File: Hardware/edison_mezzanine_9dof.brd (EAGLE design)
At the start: 30.5 x 44.5 mm, 37 parts, among them U1 LSM9DS0, U2 EDISON_CONNECTOR_FULLMOUNTING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, U3 EDISON_CONNECTOR_FULLHEADER

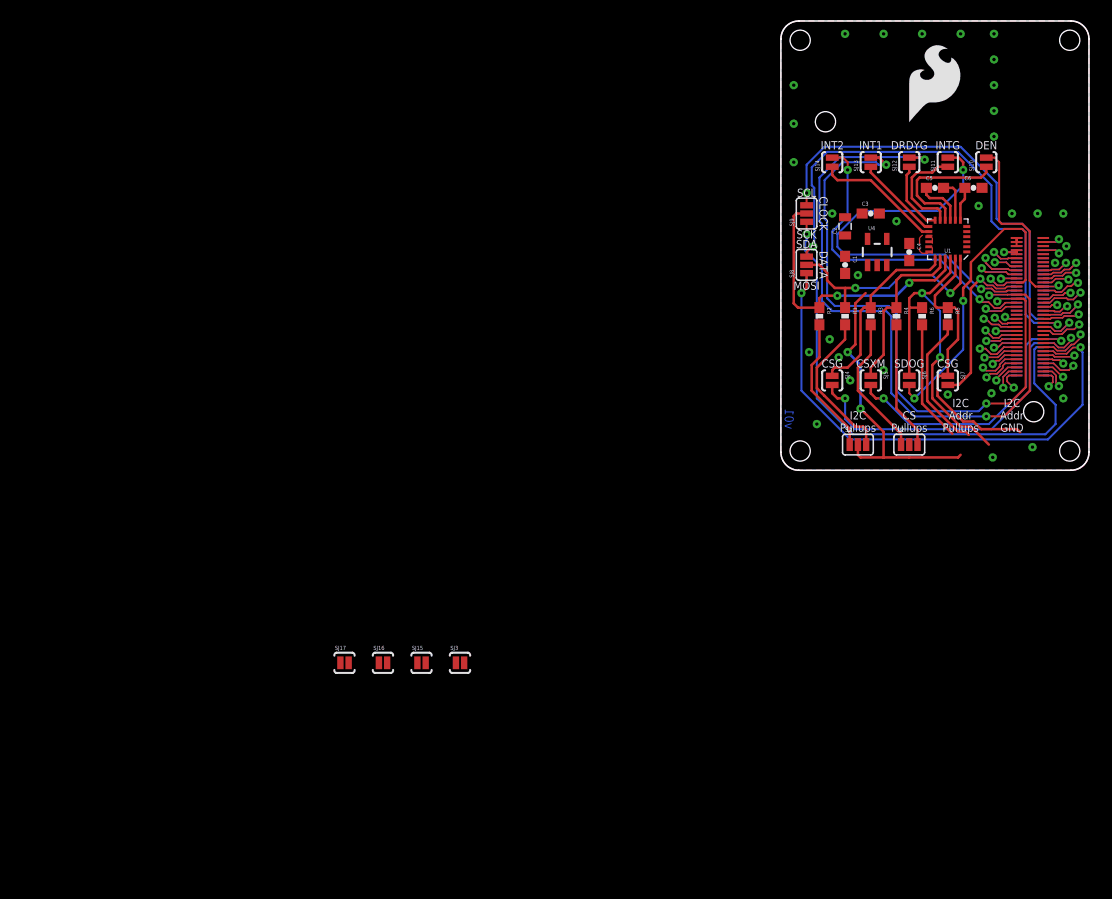
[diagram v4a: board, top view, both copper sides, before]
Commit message: Re-did power section to include LDO. Added 4x 2-way jumpers to layout for pullups/pulldowns.
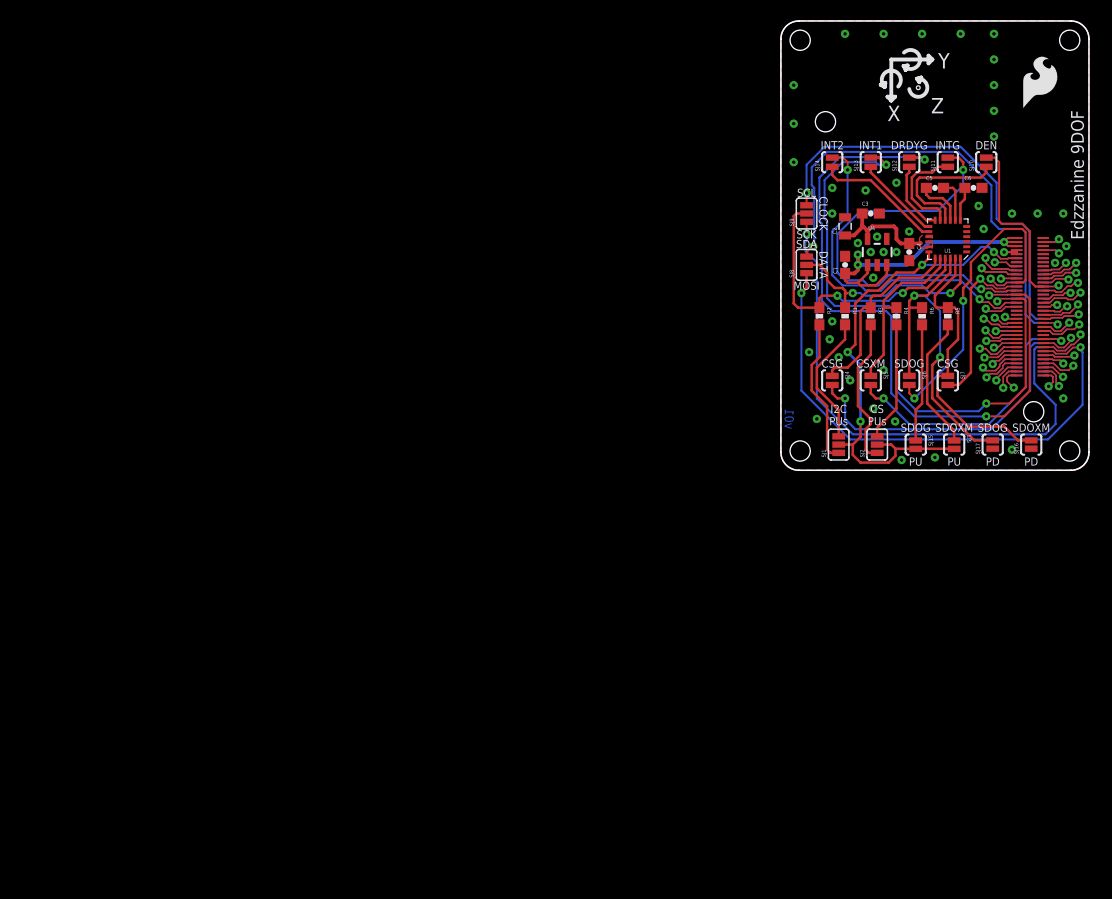
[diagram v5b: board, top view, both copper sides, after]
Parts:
- LOGO1: value SFE_LOGO_FLAME.3_INCH -> SFE_LOGO_FLAME.2_INCH; device SparkFun-Aesthetics:SFE_LOGO_FLAME_.3 -> SparkFun-Aesthetics:SFE_LOGO_FLAME_.2
- moved SJ16 67.7 mm to (24.8, 2.54), turned to 90 degrees
- moved SJ17 67.7 mm to (21.0, 2.54), turned to 90 degrees
- moved SJ15 53.4 mm to (13.3, 2.54), turned to 270 degrees
- moved SJ3 53.4 mm to (17.1, 2.54), turned to 270 degrees
- moved LOGO1 11.5 mm to (23.6, 35.6)
- moved SJ2 3.17 mm to (9.53, 2.54), turned to 90 degrees
- moved SJ1 1.91 mm to (5.71, 2.54), turned to 90 degrees
- turned C1 to 90 degrees
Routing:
- net VSYS: track 1.20 -> 36.1 mm, vias 0 -> 3
- net 1.8V: track 34.9 -> 53.7 mm, vias 3 -> 4
- net 3.3V_LOCAL: track 0.00 -> 11.6 mm
- net N$6: track 15.5 -> 13.1 mm
- net GP49: track 36.1 -> 38.4 mm
- net GP46: track 43.1 -> 45.4 mm
- net SDO_XM: track 27.4 -> 28.9 mm
- net N$5: track 12.7 -> 11.8 mm
- net N$7: track 13.7 -> 14.6 mm
- net N$4: track 14.1 -> 14.9 mm
- net SDO_G: track 34.4 -> 35.2 mm
- net SDA: track 22.7 -> 22.1 mm
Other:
- board text added: "CS PUs"
- board text added: "I2C PUs"
- board text added: "PD"
- board text added: "PU"
- board text added: "SDOXM"
- board text added: "X"
- board text added: "Y"
- board text added: "Z"
- board text removed: "CS Pullups"
- board text removed: "I2C Addr GND"
- board text removed: "I2C Addr Pullups"
- board text removed: "I2C Pullups"

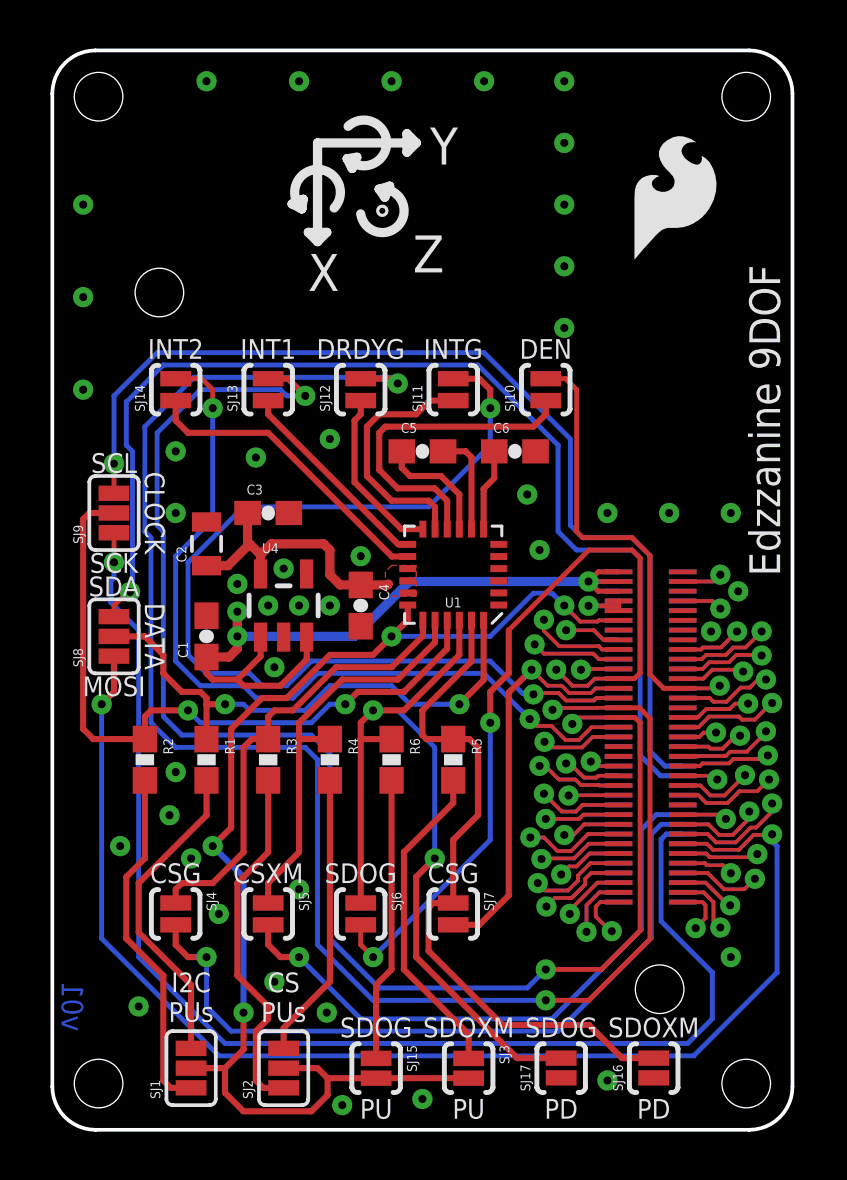
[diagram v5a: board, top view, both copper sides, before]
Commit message: Added fiducials and moved ver text on layout. Moved address table near pullups/pulldowns on schematic.
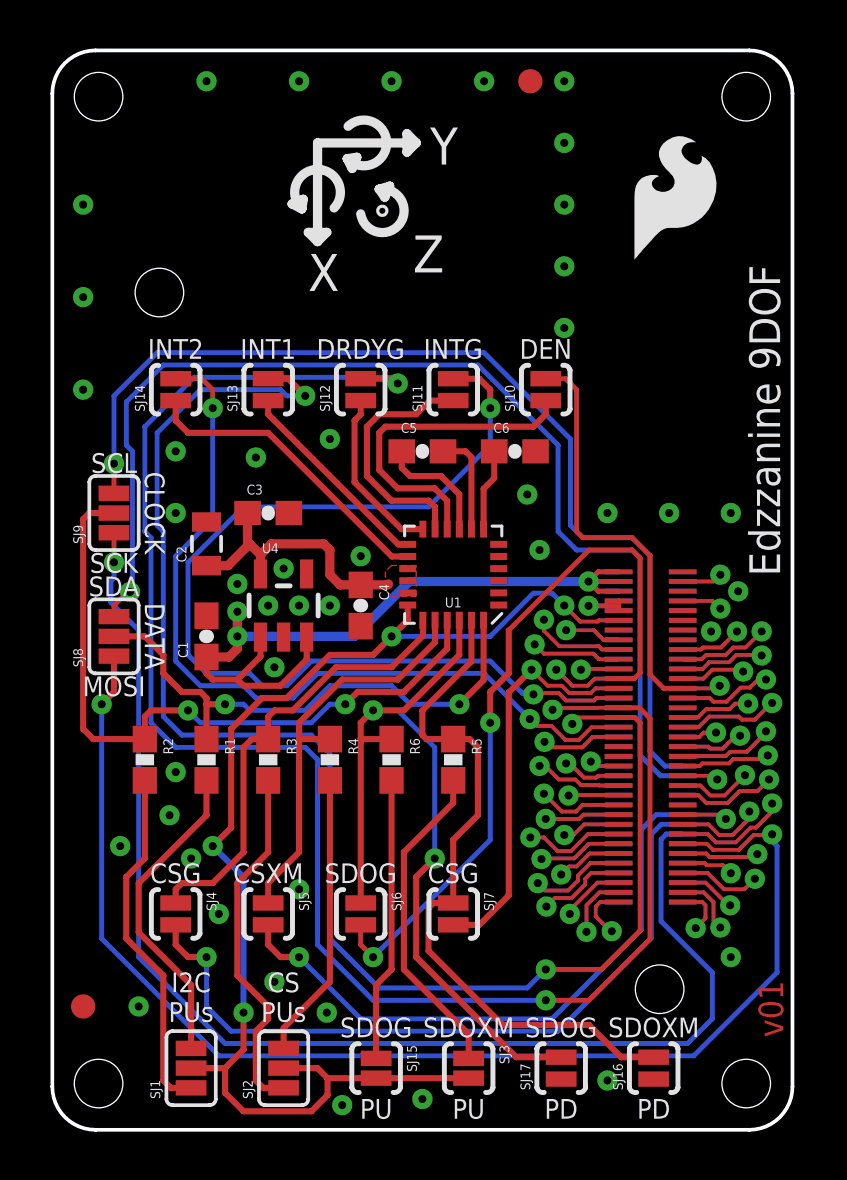
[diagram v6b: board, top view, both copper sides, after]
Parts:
- added FID1, FID2: FIDUCIAL1X2, SparkFun-Aesthetics:FIDUCIAL-1X2
- added FRAME2, FRAME3: FRAME-LETTER, SparkFun-Aesthetics:CREATIVE_COMMONS
- SJ16, SJ17: value JUMPER-PAD-2-NC_BY_PASTE -> JUMPER-PAD-2-NOYES_SILK; device SparkFun-Passives:PAD-JUMPER-2-NC_BY_PASTE_YES_SILK -> SparkFun-Passives:PAD-JUMPER-2-NO_YES_SILK
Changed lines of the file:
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@@
 <layer number="2" name="Route2" color="1" fill="3" visible="no" active="yes"/>
 <layer number="15" name="Route15" color="4" fill="6" visible="no" active="yes"/>
-<layer number="16" name="Bottom" color="1" fill="1" visible="no" active="yes"/>
+<layer number="16" name="Bottom" color="1" fill="1" visible="yes" active="yes"/>
 <layer number="17" name="Pads" color="2" fill="1" visible="yes" active="yes"/>
 <layer number="18" name="Vias" color="2" fill="1" visible="yes" active="yes"/>
@@
 <layer number="20" name="Dimension" color="15" fill="1" visible="yes" active="yes"/>
 <layer number="21" name="tPlace" color="16" fill="1" visible="yes" active="yes"/>
-<layer number="22" name="bPlace" color="14" fill="1" visible="no" active="yes"/>
+<layer number="22" name="bPlace" color="14" fill="1" visible="yes" active="yes"/>
 <layer number="23" name="tOrigins" color="15" fill="1" visible="yes" active="yes"/>
-<layer number="24" name="bOrigins" color="15" fill="1" visible="no" active="yes"/>
+<layer number="24" name="bOrigins" color="15" fill="1" visible="yes" active="yes"/>
 <layer number="25" name="tNames" color="7" fill="1" visible="no" active="yes"/>
 <layer number="26" name="bNames" color="7" fill="1" visible="no" active="yes"/>
@@
 <layer number="43" name="vRestrict" color="2" fill="10" visible="no" active="yes"/>
 <layer number="44" name="Drills" color="7" fill="1" visible="no" active="yes"/>
-<layer number="45" name="Holes" color="7" fill="1" visible="no" active="yes"/>
+<layer number="45" name="Holes" color="7" fill="1" visible="yes" active="yes"/>
 <layer number="46" name="Milling" color="3" fill="1" visible="no" active="yes"/>
-<layer number="51" name="tDocu" color="6" fill="1" visible="no" active="yes"/>
+<layer number="51" name="tDocu" color="6" fill="1" visible="yes" active="yes"/>
 <layer number="52" name="bDocu" color="7" fill="1" visible="no" active="yes"/>
 <layer number="3" name="Route3" color="4" fill="3" visible="no" active="no"/>
@@
 <text x="29.21" y="6.35" size="1.016" layer="22" font="vector" ratio="15" rot="MR90" align="center">4xM2.0</text>
 <rectangle x1="15.24" y1="21.59" x2="17.78" y2="24.13" layer="41"/>
-<text x="1.27" y="5.08" size="0.889" layer="16" font="vector" ratio="15" rot="MR90" align="top-center">v01</text>
-<rectangle x1="0.254" y1="4.318" x2="0.508" y2="4.572" layer="42"/>
 <text x="5.715" y="4.445" size="0.8128" layer="21" font="vector" ratio="15" align="bottom-center">I2C
 PUs</text>
@@
 <wire x1="14.605" y1="40.259" x2="14.605" y2="41.021" width="0.381" layer="21"/>
 <wire x1="14.986" y1="40.64" x2="14.605" y2="40.259" width="0.381" layer="21"/>
+<text x="30.099" y="3.81" size="1.016" layer="1" font="vector" ratio="14" rot="R90">v01</text>
 </plain>
 <attributes>
@@
 <element name="SJ3" library="SparkFun-Passives" package="PAD-JUMPER-2-NC_BY_PASTE_YES_SILK" value="JUMPER-PAD-2-NC_BY_PASTE" x="17.145" y="2.54" rot="R270"/>
 <element name="SJ15" library="SparkFun-Passives" package="PAD-JUMPER-2-NC_BY_PASTE_YES_SILK" value="JUMPER-PAD-2-NC_BY_PASTE" x="13.335" y="2.54" rot="R270"/>
-<element name="SJ16" library="SparkFun-Passives" package="PAD-JUMPER-2-NC_BY_PASTE_YES_SILK" value="JUMPER-PAD-2-NC_BY_PASTE" x="24.765" y="2.54" rot="R90"/>
-<element name="SJ17" library="SparkFun-Passives" package="PAD-JUMPER-2-NC_BY_PASTE_YES_SILK" value="JUMPER-PAD-2-NC_BY_PASTE" x="20.955" y="2.54" rot="R90"/>
 <element name="LOGO1" library="SparkFun-Aesthetics" package="SFE_LOGO_FLAME_.2" value="SFE_LOGO_FLAME.2_INCH" x="23.622" y="35.56"/>
+<element name="FID1" library="SparkFun-Aesthetics" package="FIDUCIAL-1X2" value="FIDUCIAL1X2" x="1.27" y="5.08"/>
+<element name="FID2" library="SparkFun-Aesthetics" package="FIDUCIAL-1X2" value="FIDUCIAL1X2" x="19.685" y="43.18"/>
+<element name="FRAME2" library="SparkFun-Aesthetics" package="CREATIVE_COMMONS" value="FRAME-LETTER" x="-8.89" y="-20.32"/>
+<element name="FRAME3" library="SparkFun-Aesthetics" package="CREATIVE_COMMONS" value="FRAME-LETTER" x="-8.89" y="-20.32"/>
+<element name="SJ16" library="SparkFun-Passives" package="PAD-JUMPER-2-NO_YES_SILK" value="JUMPER-PAD-2-NOYES_SILK" x="24.765" y="2.54" rot="R90"/>
+<element name="SJ17" library="SparkFun-Passives" package="PAD-JUMPER-2-NO_YES_SILK" value="JUMPER-PAD-2-NOYES_SILK" x="20.955" y="2.54" rot="R90"/>
 </elements>
 <signals>
@@
 <via x="22.86" y="25.4" extent="1-16" drill="0.3302"/>
 <via x="19.558" y="26.162" extent="1-16" drill="0.3302"/>
-<contactref element="SJ16" pad="1"/>
-<contactref element="SJ17" pad="1"/>
 <via x="8.89" y="21.59" extent="1-16" drill="0.3302"/>
 <via x="10.16" y="21.59" extent="1-16" drill="0.3302"/>
@@
 <via x="5.08" y="14.732" extent="1-16" drill="0.3302"/>
 <via x="20.066" y="23.876" extent="1-16" drill="0.3302"/>
+<contactref element="SJ16" pad="1"/>
+<contactref element="SJ17" pad="1"/>
 </signal>
 <signal name="VSYS">
@@
 <wire x1="13.97" y1="16.09" x2="12.7136" y2="16.09" width="0.254" layer="1"/>
 <wire x1="12.7136" y1="16.09" x2="12.7" y2="16.1036" width="0.254" layer="1"/>
-<contactref element="SJ17" pad="2"/>
-<wire x1="20.955" y1="2.9527" x2="19.1453" y2="2.9527" width="0.254" layer="1"/>
-<wire x1="19.1453" y1="2.9527" x2="14.986" y2="7.112" width="0.254" layer="1"/>
 <wire x1="14.478" y1="17.272" x2="16.76" y2="19.554" width="0.254" layer="1"/>
 <wire x1="12.7" y1="16.1036" x2="12.7" y2="16.764" width="0.254" layer="1"/>
@@
 <wire x1="15.748" y1="15.748" x2="14.224" y2="17.272" width="0.2032" layer="16"/>
 <wire x1="14.224" y1="17.272" x2="13.208" y2="17.272" width="0.2032" layer="16"/>
+<contactref element="SJ17" pad="2"/>
+<wire x1="20.955" y1="2.99" x2="19.108" y2="2.99" width="0.254" layer="1"/>
+<wire x1="19.108" y1="2.99" x2="14.986" y2="7.112" width="0.254" layer="1"/>
 </signal>
 <signal name="CS_XM">
@@
 <wire x1="15.406" y1="16.09" x2="15.24" y2="16.256" width="0.254" layer="1"/>
 <wire x1="15.24" y1="16.256" x2="15.24" y2="17.272" width="0.254" layer="1"/>
+<wire x1="15.494" y1="7.366" x2="18.542" y2="4.318" width="0.254" layer="1"/>
+<wire x1="22.098" y1="4.318" x2="18.542" y2="4.318" width="0.254" layer="1"/>
 <contactref element="SJ16" pad="2"/>
-<wire x1="15.494" y1="7.366" x2="18.542" y2="4.318" width="0.254" layer="1"/>
-<wire x1="24.765" y1="2.9527" x2="23.4633" y2="2.9527" width="0.254" layer="1"/>
-<wire x1="23.4633" y1="2.9527" x2="22.098" y2="4.318" width="0.254" layer="1"/>
-<wire x1="22.098" y1="4.318" x2="18.542" y2="4.318" width="0.254" layer="1"/>
+<wire x1="24.765" y1="2.99" x2="23.426" y2="2.99" width="0.254" layer="1"/>
+<wire x1="23.426" y1="2.99" x2="22.098" y2="4.318" width="0.254" layer="1"/>
 </signal>
 <signal name="N$4">
